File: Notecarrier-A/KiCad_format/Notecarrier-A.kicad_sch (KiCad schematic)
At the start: 60 parts, among them J19 MICROUSB-B, J20 MDT420E01001, J21 NU, J22 NU, J23 S2B-PH-SM4-TB(LF)(SN), J24 SM04B-SRSS-TBT, Q2 AO3420, U3 MAX17225ELT, U4 TPS62748YFPT, U5 MCP73831-2ACI/MC

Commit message: Add first pass of port of Notecarrier-A Power sheet.
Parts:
- removed C10, C111, C115, C116, C7: 100n/16V, blues-kicad-lib:CS-C-0402, symbol Device:C_Small
- removed C112: 10n/1kV, blues-kicad-lib:CS-C-1206, symbol Device:C_Small
- removed C113: NU, blues-kicad-lib:CS-T-A, symbol Device:C_Polarized_Small
- removed C114: NU, blues-kicad-lib:CS-T-B, symbol Device:C_Polarized_Small
- removed C117, C118: 4.7u/10V/X5R, blues-kicad-lib:CS-C-0603, symbol Device:C_Small
- removed C13: 47u/16V-X5R, blues-kicad-lib:CS-C-1206, symbol Device:C_Small
- removed C14: 4.7u/6.3V-X5R, blues-kicad-lib:CS-C-0402, symbol Device:C_Small
- removed C15, C16: 10u/10V-X5R, blues-kicad-lib:CS-C-0603, symbol Device:C_Small
- removed C8, C9: 10u/6.3V-X5R, blues-kicad-lib:CS-C-0402, symbol Device:C_Small
- removed DS14: STPS3H100U, blues-kicad-lib:SMB, symbol Device:D_Schottky_Filled
- removed DS15: FSV1045V, blues-kicad-lib:TO277-3, symbol blues-kicad-lib:FSV1045V
- removed DSW1: DIP-SW-CHS-01TB, blues-kicad-lib:DSS-CHS-01TB, symbol Switch:SW_DIP_x01
- removed F1: SF-0603F150-2, blues-kicad-lib:FS-0603, symbol Device:Fuse
- removed F2: 3.5A/32V, blues-kicad-lib:FS-0603, symbol Device:Fuse
- removed J19: MICROUSB-B, blues-kicad-lib:J-5-0065-FOS-MICROUSB10118192, symbol Connector:USB_B_Micro
- removed J20: MDT420E01001, blues-kicad-lib:J-75-0050-MOS-M2-E, symbol blues-kicad-lib:MDT420E01001
- removed J21, J22: NU, blues-kicad-lib:J-10-0254-MDT, symbol Connector_Generic:Conn_01x10
- removed J23: S2B-PH-SM4-TB(LF)(SN), blues-kicad-lib:J-2-0200-MOS-S2B, symbol blues-kicad-lib:S2B-PH-SM4-TB(LF)(SN)
- removed J24: SM04B-SRSS-TBT, blues-kicad-lib:J-4-0100-MOS-SH, symbol Connector_Generic:Conn_01x04
- removed L2: 1285AS-H-2R2M=P2, blues-kicad-lib:LS-0806, symbol Device:L
- removed L4: XFL4020-222MEC, blues-kicad-lib:LS-XFL4020, symbol blues-kicad-lib:L_Shielded
- removed LD1: SML-P12WTT86R, blues-kicad-lib:LD-0402, symbol blues-kicad-lib:LED_Filled_Yellow
- removed Q2: AO3420, blues-kicad-lib:SOT23, symbol blues-kicad-lib:AO3420
- removed R10: 10M/5%, blues-kicad-lib:RS-0402, symbol Device:R
- removed R307: 1M, blues-kicad-lib:RS-1206, symbol Device:R
- removed R318, R322, R325: 0R, blues-kicad-lib:RS-0402, symbol Device:R
- removed R319: 1k, blues-kicad-lib:RS-0402, symbol Device:R
- removed R323, R324, R326: NU, blues-kicad-lib:RS-0402, symbol Device:R
- removed R5: 1k, blues-kicad-lib:RS-0201, symbol Device:R
- removed R6: 82k, blues-kicad-lib:RS-0402, symbol Device:R
- removed R7: 2.8k, blues-kicad-lib:RS-0201, symbol Device:R
- removed TVS1: SM6T6V8A, blues-kicad-lib:SMB, symbol Diode:SM6T6V8A
- removed U3: MAX17225ELT, blues-kicad-lib:WDFN6-0200X0200, symbol blues-kicad-lib:MAX17225ELT
- removed U4: TPS62748YFPT, blues-kicad-lib:XFBGA8, symbol blues-kicad-lib:TPS62748
- removed U5: MCP73831-2ACI/MC, blues-kicad-lib:VFDFN8-EXP, symbol blues-kicad-lib:MCP73831-2ACI/MC
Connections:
- no-connect marks 54 -> 21
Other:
- added sheet Connector (Notecarrier-A_Connector.kicad_sch)
- added sheet Power (Notecarrier-A_Power.kicad_sch)
- note removed: "150mA"
- note removed: "180mA"
- note removed: "Diode OR"
- note removed: "Edge Connector"
- note removed: "F1.5A"
- note removed: "G=Giallo (Yellow)"
- note removed: "Li-po Battery 3.3V - 4.2V"
- note removed: "LiPo Charger"
- note removed: "Notecard Connector"
- note removed: "Power"
- note removed: "Qwiic Connector"

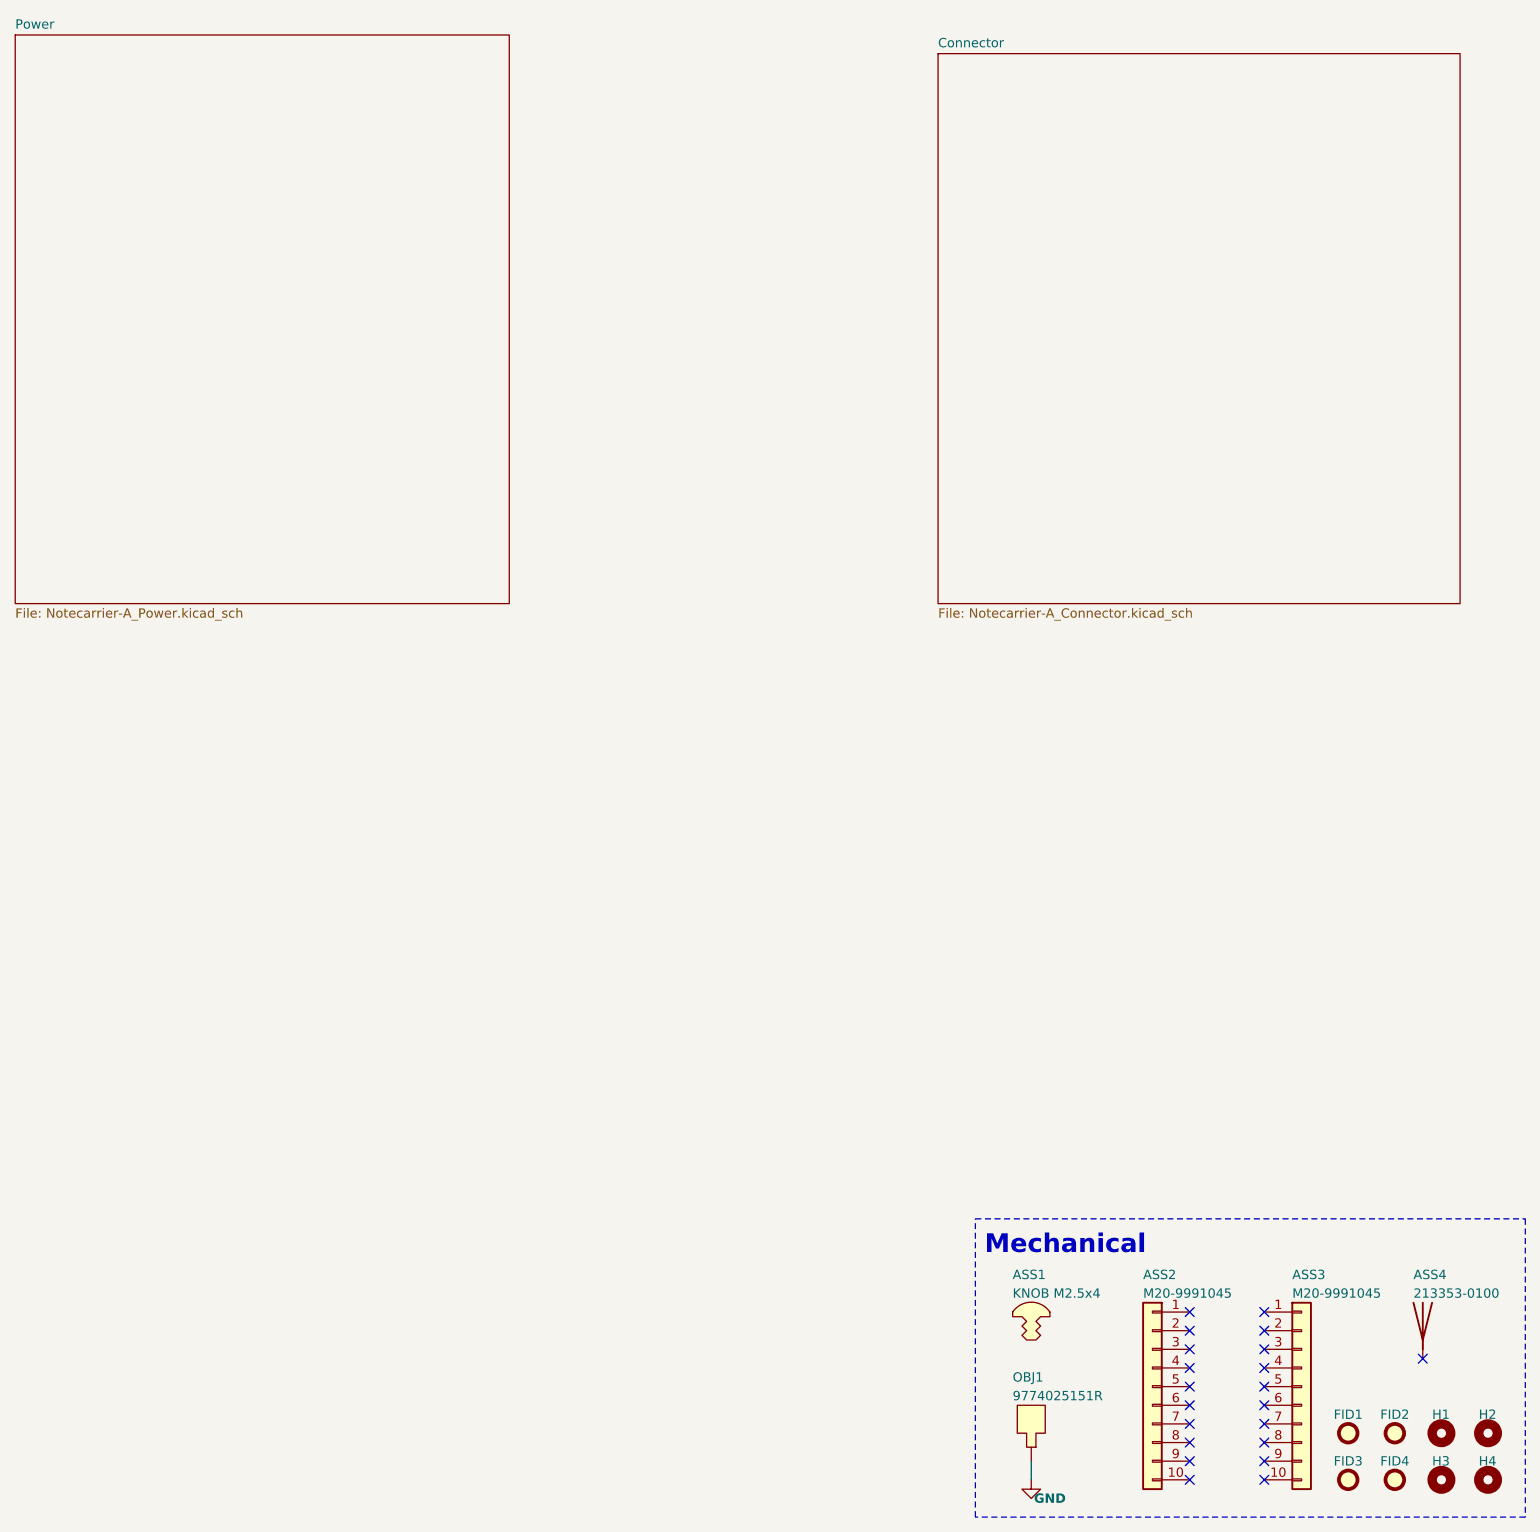
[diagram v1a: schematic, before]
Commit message: Add first pass of port of Notecarrier-A Connector sheet.
First pass port of schematics now complete. Next step: BOM.
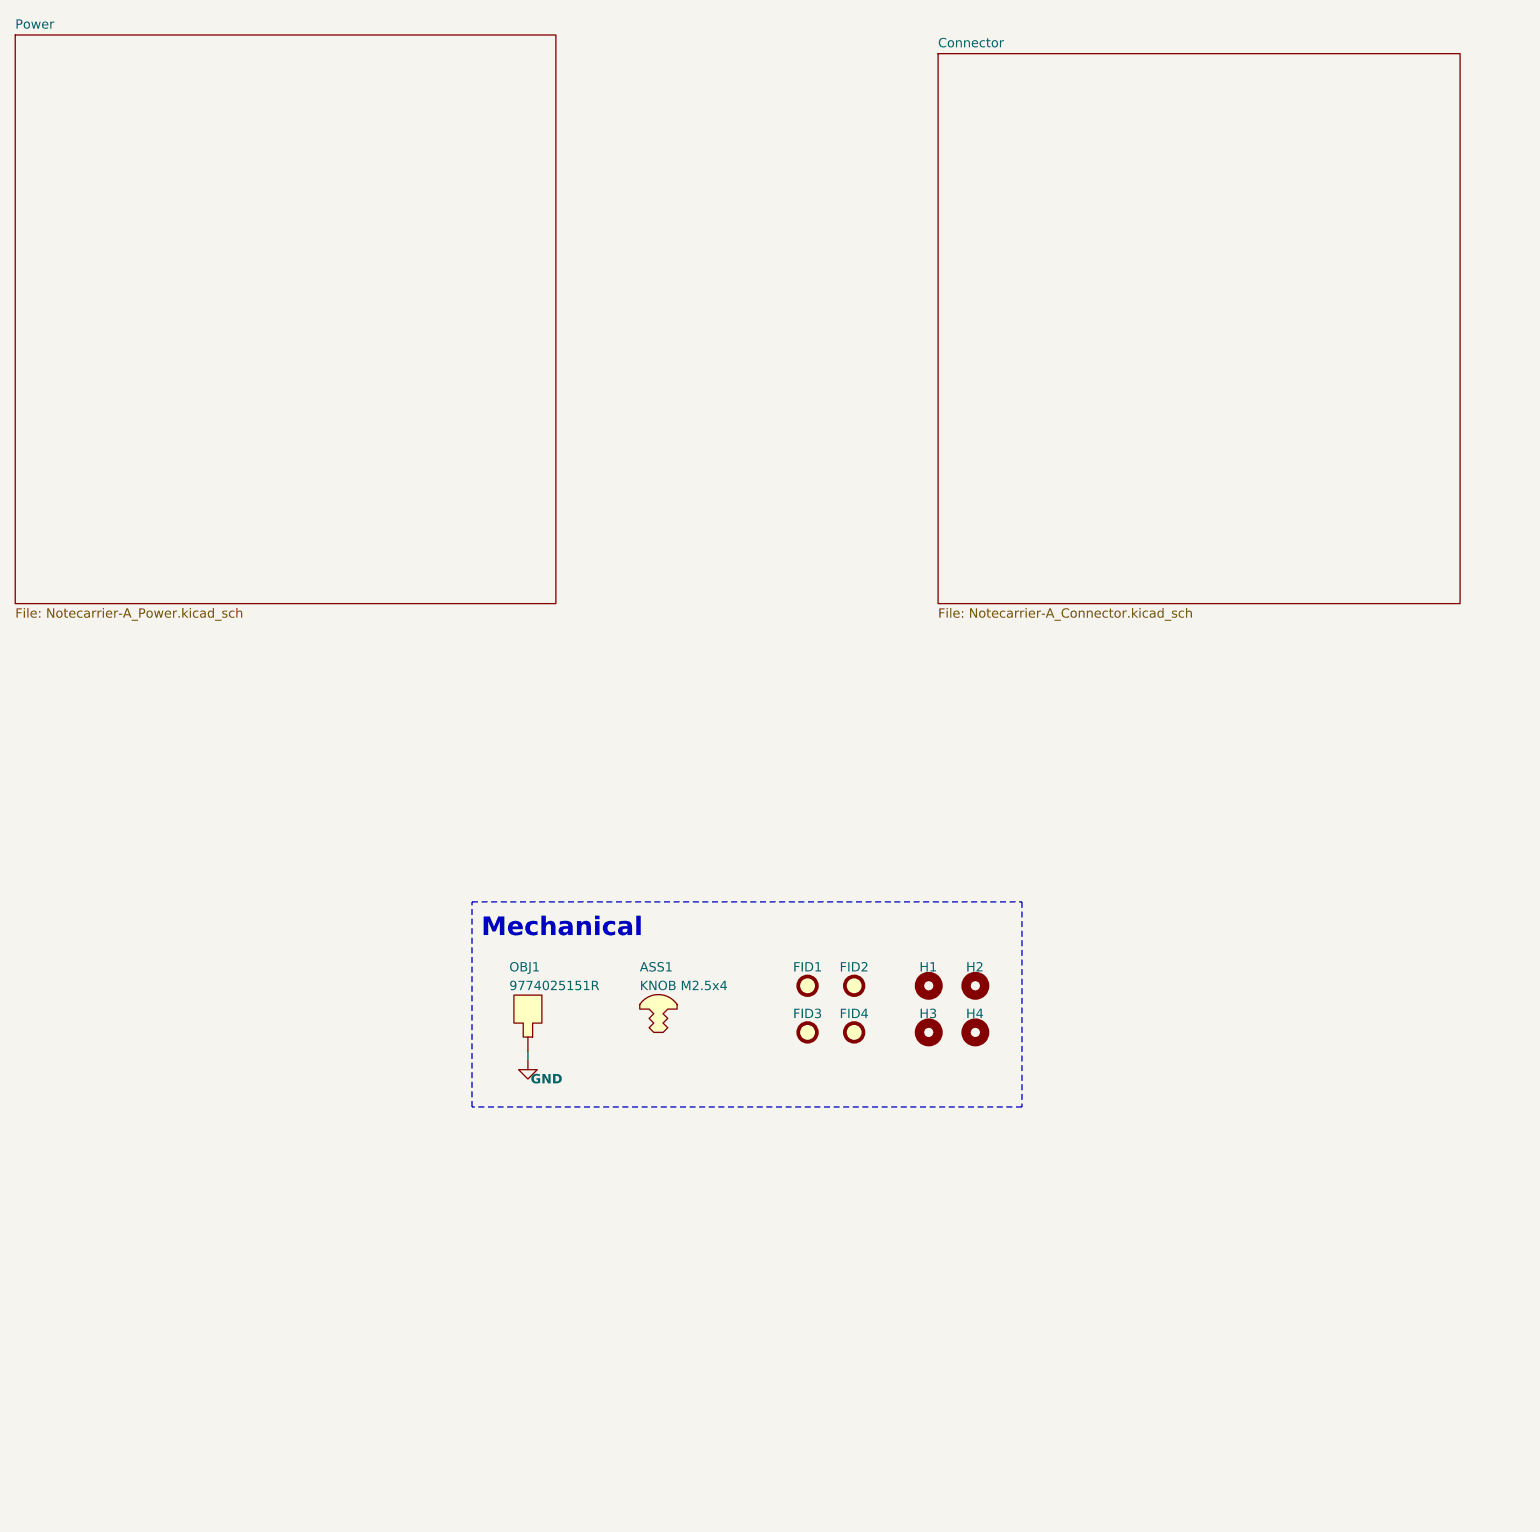
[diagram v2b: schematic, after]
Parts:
- removed ASS2, ASS3: M20-9991045, symbol Connector_Generic:Conn_01x10
- removed ASS4: 213353-0100, symbol Device:Antenna
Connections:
- no-connect marks 21 -> 0
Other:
- moved on the sheet: ASS1, FID1, FID2, FID3, FID4, H1, H2, H3, H4, OBJ1

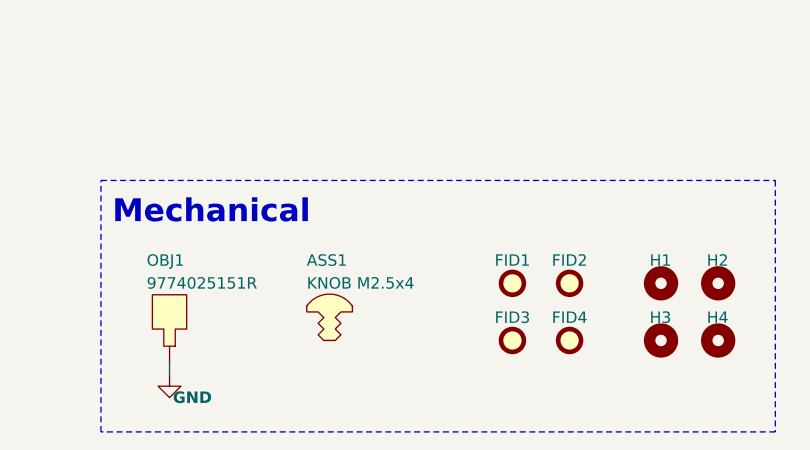
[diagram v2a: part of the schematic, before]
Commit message: Establish port of Notecarrier-B PCB.
Ported: components, board outline, fabrication layers, silkscreens and front copper.
To go: inner and back copper layers, drills, sheet metadata.
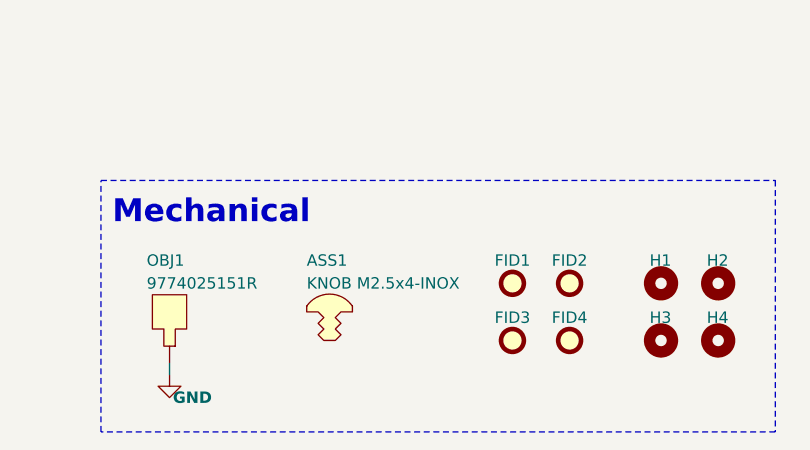
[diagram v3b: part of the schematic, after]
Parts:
- ASS1: value KNOB M2.5x4 -> KNOB M2.5x4-INOX; Caratteristiche (none) -> M2.5; Distributor (none) -> FAE
- FID1, FID2, FID3, FID4: Distributor (none) -> FAE
- OBJ1: Caratteristiche (none) -> M2.5; Distributor (none) -> FAE
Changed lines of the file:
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@@
+      (effects (font (size 1.27 1.27)) hide)
+    )
+    (property "Caratteristiche" "M2.5" (at 173.99 212.09 0)
+      (effects (font (size 1.27 1.27)) hide)
+    )
+    (property "Distributor" "FAE" (at 173.99 212.09 0)
       (effects (font (size 1.27 1.27)) hide)
     )
@@
     )
     (property "Pkg Type" "SMD" (at 218.44 213.36 0)
+      (effects (font (size 1.27 1.27)) hide)
+    )
+    (property "Distributor" "FAE" (at 218.44 213.36 0)
       (effects (font (size 1.27 1.27)) hide)
     )
@@
       (effects (font (size 1.27 1.27)) (justify left))
     )
-    (property "Value" "KNOB M2.5x4" (at 189.23 207.01 0)
+    (property "Value" "KNOB M2.5x4-INOX" (at 189.23 207.01 0)
       (effects (font (size 1.27 1.27)) (justify left))
     )
@@
       (effects (font (size 1.27 1.27)) hide)
     )
-    (property "Description" "SCREW TCEI 2.5X4 DIN 7985 PHILIPS" (at 191.77 210.82 0)
+    (property "Description" "SCREW CYLINDRICAL HEAD HEX SOCKET 2.5X4 A2 INOX" (at 191.77 210.82 0)
       (effects (font (size 1.27 1.27)) hide)
     )
@@
       (effects (font (size 1.27 1.27)) hide)
     )
-    (property "Critical" "" (at 191.77 210.82 0)
-      (effects (font (size 1.27 1.27)) hide)
-    )
-    (property "Manufacturer" "" (at 191.77 210.82 0)
-      (effects (font (size 1.27 1.27)) hide)
-    )
-    (property "Order Code" "" (at 191.77 210.82 0)
-      (effects (font (size 1.27 1.27)) hide)
-    )
-    (property "Part Number" "" (at 191.77 210.82 0)
-      (effects (font (size 1.27 1.27)) hide)
-    )
-    (property "Supplier" "" (at 191.77 210.82 0)
+    (property "Caratteristiche" "M2.5" (at 191.77 210.82 0)
+      (effects (font (size 1.27 1.27)) hide)
+    )
+    (property "Distributor" "FAE" (at 191.77 210.82 0)
       (effects (font (size 1.27 1.27)) hide)
     )
@@
       (effects (font (size 1.27 1.27)) hide)
     )
-    (property "Critical" "" (at 212.09 213.36 0)
-      (effects (font (size 1.27 1.27)) hide)
-    )
-    (property "Manufacturer" "" (at 212.09 213.36 0)
-      (effects (font (size 1.27 1.27)) hide)
-    )
-    (property "Order Code" "" (at 212.09 213.36 0)
-      (effects (font (size 1.27 1.27)) hide)
-    )
-    (property "Part Number" "" (at 212.09 213.36 0)
-      (effects (font (size 1.27 1.27)) hide)
-    )
-    (property "Supplier" "" (at 212.09 213.36 0)
+    (property "Distributor" "FAE" (at 212.09 213.36 0)
       (effects (font (size 1.27 1.27)) hide)
     )
@@
       (effects (font (size 1.27 1.27)) hide)
     )
-    (property "Critical" "" (at 228.6 213.36 0)
-      (effects (font (size 1.27 1.27)) hide)
-    )
     (property "Description" "" (at 228.6 213.36 0)
       (effects (font (size 1.27 1.27)) hide)
     )
-    (property "Manufacturer" "" (at 228.6 213.36 0)
-      (effects (font (size 1.27 1.27)) hide)
-    )
-    (property "Order Code" "" (at 228.6 213.36 0)
-      (effects (font (size 1.27 1.27)) hide)
-    )
-    (property "Part Number" "" (at 228.6 213.36 0)
-      (effects (font (size 1.27 1.27)) hide)
-    )
-    (property "Supplier" "" (at 228.6 213.36 0)
+    (property "Distributor" "" (at 228.6 213.36 0)
       (effects (font (size 1.27 1.27)) hide)
     )
@@
       (effects (font (size 1.27 1.27)) hide)
     )
-    (property "Critical" "" (at 234.95 213.36 0)
-      (effects (font (size 1.27 1.27)) hide)
-    )
     (property "Description" "" (at 234.95 213.36 0)
       (effects (font (size 1.27 1.27)) hide)
     )
-    (property "Manufacturer" "" (at 234.95 213.36 0)
-      (effects (font (size 1.27 1.27)) hide)
-    )
-    (property "Order Code" "" (at 234.95 213.36 0)
-      (effects (font (size 1.27 1.27)) hide)
-    )
-    (property "Part Number" "" (at 234.95 213.36 0)
-      (effects (font (size 1.27 1.27)) hide)
-    )
-    (property "Supplier" "" (at 234.95 213.36 0)
+    (property "Distributor" "" (at 234.95 213.36 0)
       (effects (font (size 1.27 1.27)) hide)
     )
@@
       (effects (font (size 1.27 1.27)) hide)
     )
-    (property "Critical" "" (at 228.6 207.01 0)
-      (effects (font (size 1.27 1.27)) hide)
-    )
     (property "Description" "" (at 228.6 207.01 0)
       (effects (font (size 1.27 1.27)) hide)
     )
-    (property "Manufacturer" "" (at 228.6 207.01 0)
-      (effects (font (size 1.27 1.27)) hide)
-    )
-    (property "Order Code" "" (at 228.6 207.01 0)
-      (effects (font (size 1.27 1.27)) hide)
-    )
-    (property "Part Number" "" (at 228.6 207.01 0)
-      (effects (font (size 1.27 1.27)) hide)
-    )
-    (property "Supplier" "" (at 228.6 207.01 0)
+    (property "Distributor" "" (at 228.6 207.01 0)
       (effects (font (size 1.27 1.27)) hide)
     )
@@
       (effects (font (size 1.27 1.27)) hide)
     )
+    (property "Distributor" "FAE" (at 218.44 207.01 0)
+      (effects (font (size 1.27 1.27)) hide)
+    )
     (instances
       (project "Notecarrier-A"
@@
       (effects (font (size 1.27 1.27)) hide)
     )
-    (property "Critical" "" (at 234.95 207.01 0)
-      (effects (font (size 1.27 1.27)) hide)
-    )
     (property "Description" "" (at 234.95 207.01 0)
       (effects (font (size 1.27 1.27)) hide)
     )
-    (property "Manufacturer" "" (at 234.95 207.01 0)
-      (effects (font (size 1.27 1.27)) hide)
-    )
-    (property "Order Code" "" (at 234.95 207.01 0)
-      (effects (font (size 1.27 1.27)) hide)
-    )
-    (property "Part Number" "" (at 234.95 207.01 0)
-      (effects (font (size 1.27 1.27)) hide)
-    )
-    (property "Supplier" "" (at 234.95 207.01 0)
+    (property "Distributor" "" (at 234.95 207.01 0)
       (effects (font (size 1.27 1.27)) hide)
     )
@@
       (effects (font (size 1.27 1.27)) hide)
     )
-    (property "Critical" "" (at 212.09 207.01 0)
-      (effects (font (size 1.27 1.27)) hide)
-    )
-    (property "Manufacturer" "" (at 212.09 207.01 0)
-      (effects (font (size 1.27 1.27)) hide)
-    )
-    (property "Order Code" "" (at 212.09 207.01 0)
-      (effects (font (size 1.27 1.27)) hide)
-    )
-    (property "Part Number" "" (at 212.09 207.01 0)
-      (effects (font (size 1.27 1.27)) hide)
-    )
-    (property "Supplier" "" (at 212.09 207.01 0)
-      (effects (font (size 1.27 1.27)) hide)
-    )
+    (property "Distributor" "FAE" (at 212.09 207.01 0)
+      (effects (font (size 1.27 1.27)) hide)
+    )
